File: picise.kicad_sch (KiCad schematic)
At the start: 22 parts, among them J1 SSW-120-22-G-D-RA, J2 SMA jack, J3 TSW-120-08-G-D-RA, J4 Conn_01x02, U1 CAT24C256, U2 MAX-M10S

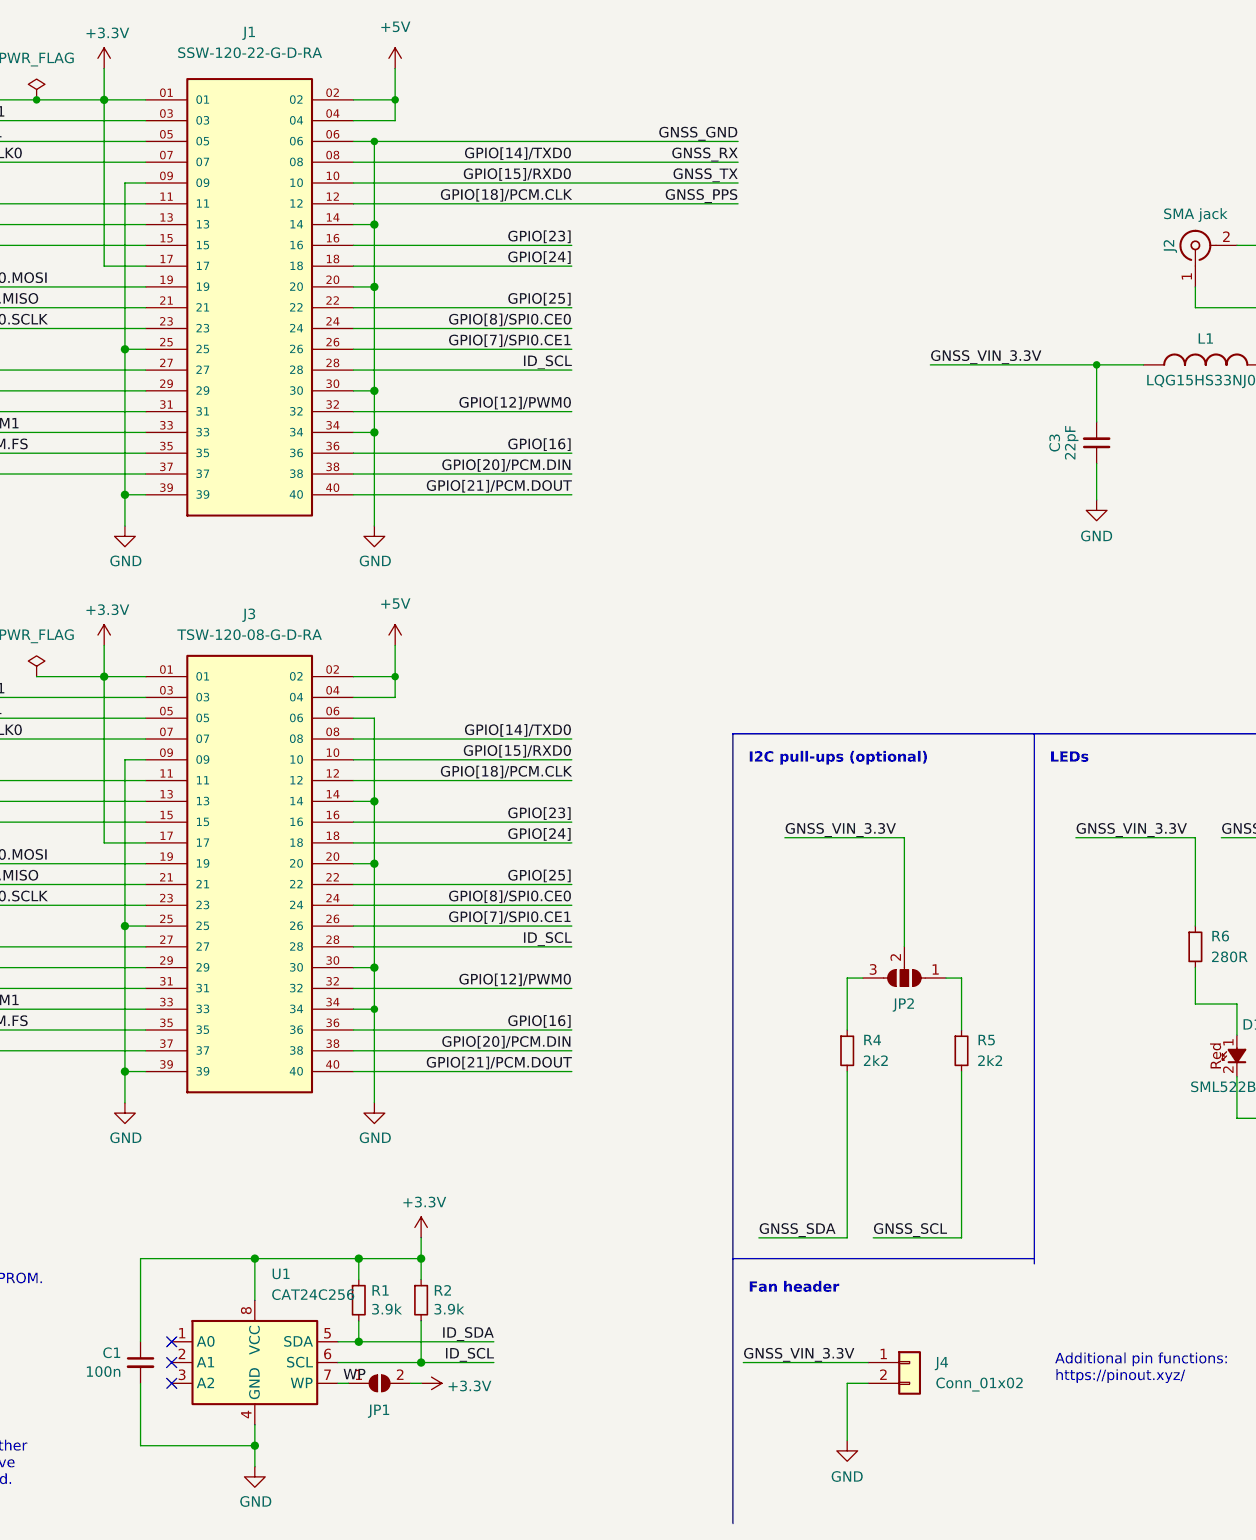
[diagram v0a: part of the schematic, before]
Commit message: added BOM
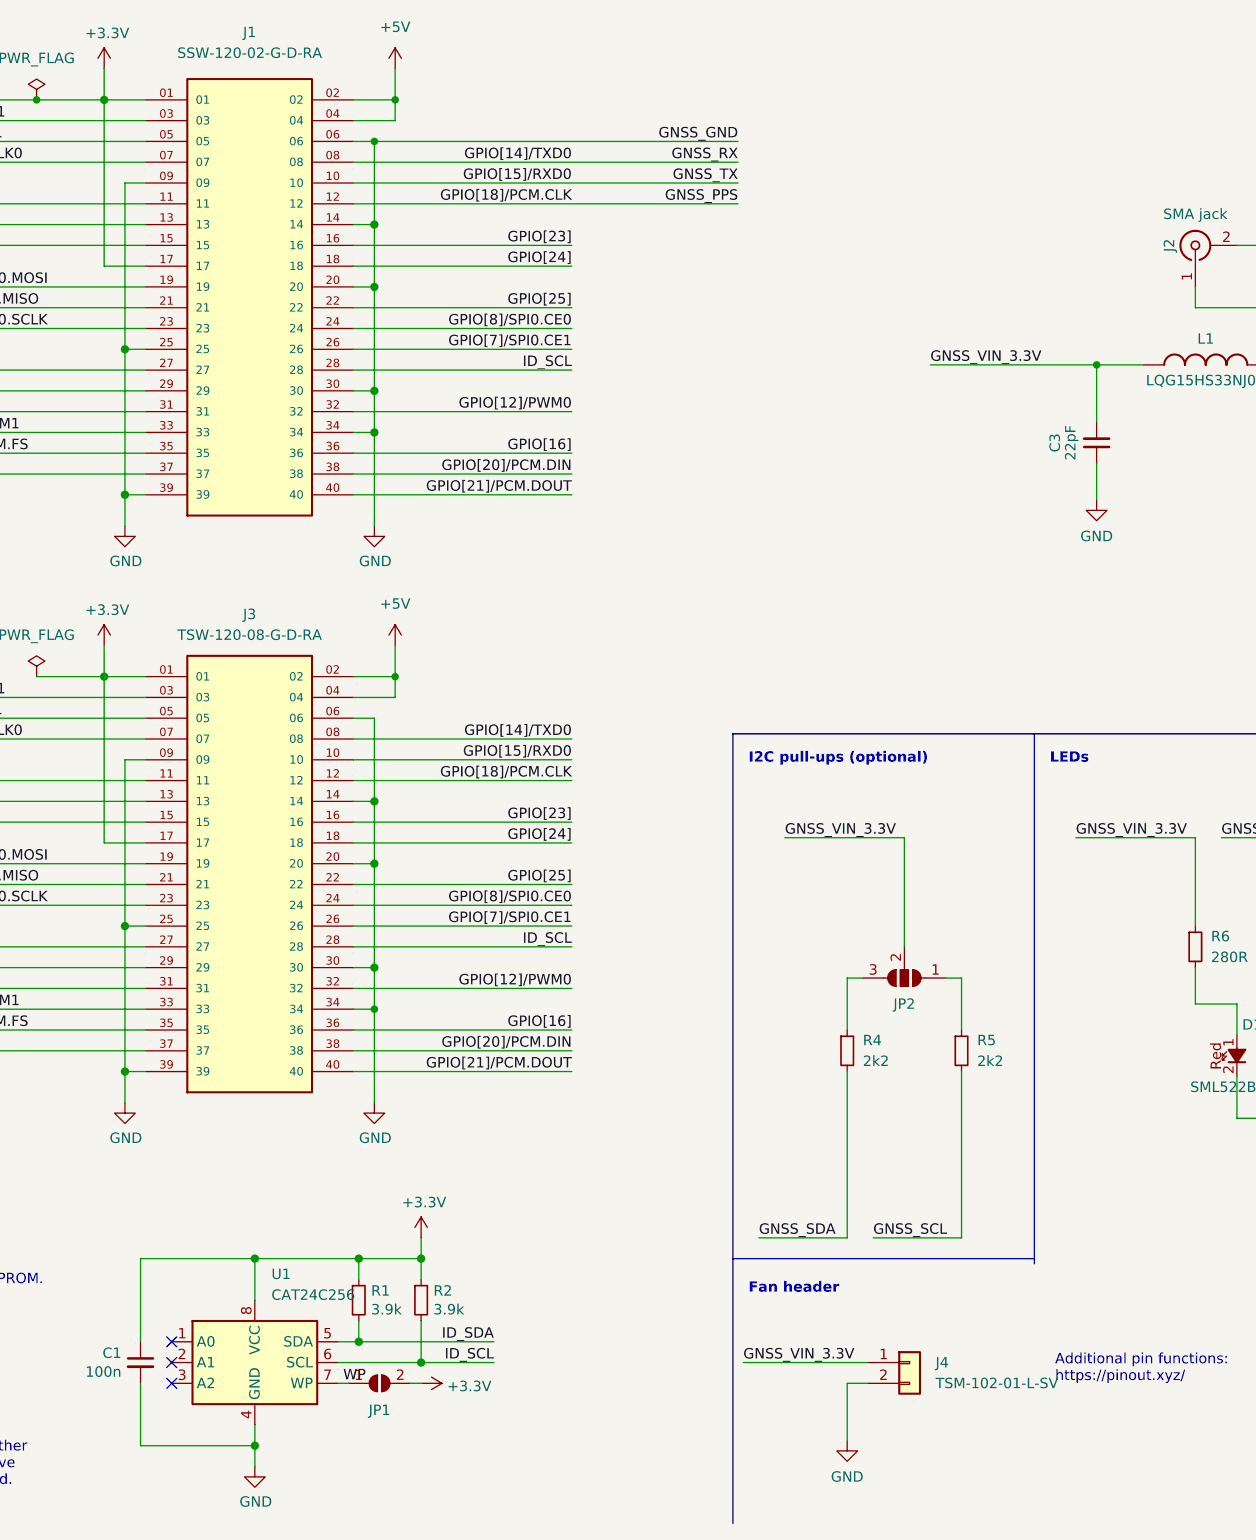
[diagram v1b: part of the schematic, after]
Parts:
- C1: MPN (none) -> C0805C104J5RAC7800; Manufacturer (none) -> KEMET
- C2: MPN (none) -> C0805C105J4RAC7800; Manufacturer (none) -> KEMET
- C3: MPN (none) -> C0805C220J4GAC7800; Manufacturer (none) -> KEMET
- D2: footprint Capacitor_SMD:C_0805_2012Metric_Pad1.18x1.45mm_HandSolder -> Diode_SMD:D_0805_2012Metric; MPN (none) -> SD0805S040S0R5; Manufacturer (none) -> KYOCERA AVX
- J1: value SSW-120-22-G-D-RA -> SSW-120-02-G-D-RA
- J4: value Conn_01x02 -> TSM-102-01-L-SV; MPN (none) -> TSM-102-01-L-SV; Manufacturer (none) -> Samtec
- R1, R2: MPN (none) -> RK73H2ARTTD3901F; Manufacturer (none) -> KOA Speer
- R3: MPN (none) -> RK73H2ATTD6200F; Manufacturer (none) -> KOA Speer
- R4, R5: MPN (none) -> RK73H2ATTD2201F; Manufacturer (none) -> KOA Speer
- R6: MPN (none) -> RK73H2ATTD2800F; Manufacturer (none) -> KOA Speer
- R7: MPN (none) -> RK73H2ARTTD80R6F; Manufacturer (none) -> KOA Speer
- U2: MPN MAX-M10S -> MAX-M10S-00B
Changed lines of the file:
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@@
+      (effects (font (size 1.27 1.27)) hide)
+    )
+    (property "MPN" "C0805C104J5RAC7800" (id 4) (at 67.31 177.8 0)
+      (effects (font (size 1.27 1.27)) hide)
+    )
+    (property "Manufacturer" "KEMET" (id 5) (at 67.31 177.8 0)
       (effects (font (size 1.27 1.27)) hide)
     )
@@
       (effects (font (size 1.27 1.27)) hide)
     )
-    (property "MPN" "MAX-M10S" (id 5) (at 250.19 76.835 0)
+    (property "MPN" "MAX-M10S-00B" (id 5) (at 250.19 76.835 0)
       (effects (font (size 1.27 1.27)) hide)
     )
@@
       (effects (font (size 1.27 1.27)) hide)
     )
+    (property "MPN" "C0805C105J4RAC7800" (id 4) (at 261.62 148.59 0)
+      (effects (font (size 1.27 1.27)) hide)
+    )
+    (property "Manufacturer" "KEMET" (id 5) (at 261.62 148.59 0)
+      (effects (font (size 1.27 1.27)) hide)
+    )
     (pin "1")
     (pin "2")
@@
     )
     (property "Datasheet" "~" (id 3) (at 93.98 170.18 0)
+      (effects (font (size 1.27 1.27)) hide)
+    )
+    (property "MPN" "RK73H2ARTTD3901F" (id 4) (at 93.98 170.18 0)
+      (effects (font (size 1.27 1.27)) hide)
+    )
+    (property "Manufacturer" "KOA Speer" (id 5) (at 93.98 170.18 0)
       (effects (font (size 1.27 1.27)) hide)
     )
@@
     )
     (property "Datasheet" "~" (id 3) (at 101.6 170.18 0)
+      (effects (font (size 1.27 1.27)) hide)
+    )
+    (property "MPN" "RK73H2ARTTD3901F" (id 4) (at 101.6 170.18 0)
+      (effects (font (size 1.27 1.27)) hide)
+    )
+    (property "Manufacturer" "KOA Speer" (id 5) (at 101.6 170.18 0)
       (effects (font (size 1.27 1.27)) hide)
     )
@@
       (effects (font (size 1.27 1.27)) (justify right))
     )
-    (property "Footprint" "Capacitor_SMD:C_0805_2012Metric_Pad1.18x1.45mm_HandSolder" (id 2) (at 240.665 123.825 0)
+    (property "Footprint" "Diode_SMD:D_0805_2012Metric" (id 2) (at 240.665 123.825 0)
       (effects (font (size 1.27 1.27)) hide)
     )
     (property "Datasheet" "~" (id 3) (at 240.665 123.825 0)
+      (effects (font (size 1.27 1.27)) hide)
+    )
+    (property "MPN" "SD0805S040S0R5" (id 4) (at 240.665 123.825 0)
+      (effects (font (size 1.27 1.27)) hide)
+    )
+    (property "Manufacturer" "KYOCERA AVX" (id 5) (at 240.665 123.825 0)
       (effects (font (size 1.27 1.27)) hide)
     )
@@
     )
     (property "Datasheet" "~" (id 3) (at 167.64 139.7 0)
+      (effects (font (size 1.27 1.27)) hide)
+    )
+    (property "MPN" "RK73H2ATTD2201F" (id 4) (at 167.64 139.7 0)
+      (effects (font (size 1.27 1.27)) hide)
+    )
+    (property "Manufacturer" "KOA Speer" (id 5) (at 167.64 139.7 0)
       (effects (font (size 1.27 1.27)) hide)
     )
@@
       (effects (font (size 1.27 1.27)) (justify left))
     )
-    (property "Value" "Conn_01x02" (id 1) (at 164.465 180.3399 0)
+    (property "Value" "TSM-102-01-L-SV" (id 1) (at 164.465 180.3399 0)
       (effects (font (size 1.27 1.27)) (justify left))
     )
@@
     )
     (property "Datasheet" "~" (id 3) (at 161.29 177.8 0)
+      (effects (font (size 1.27 1.27)) hide)
+    )
+    (property "MPN" "TSM-102-01-L-SV" (id 4) (at 161.29 177.8 0)
+      (effects (font (size 1.27 1.27)) hide)
+    )
+    (property "Manufacturer" "Samtec" (id 5) (at 161.29 177.8 0)
       (effects (font (size 1.27 1.27)) hide)
     )
@@
       (effects (font (size 1.27 1.27)) hide)
     )
+    (property "MPN" "RK73H2ATTD2201F" (id 4) (at 153.67 139.7 0)
+      (effects (font (size 1.27 1.27)) hide)
+    )
+    (property "Manufacturer" "KOA Speer" (id 5) (at 153.67 139.7 0)
+      (effects (font (size 1.27 1.27)) hide)
+    )
     (pin "1")
     (pin "2")
@@
       (effects (font (size 1.27 1.27)) hide)
     )
+    (property "MPN" "RK73H2ATTD6200F" (id 4) (at 240.665 133.985 0)
+      (effects (font (size 1.27 1.27)) hide)
+    )
+    (property "Manufacturer" "KOA Speer" (id 5) (at 240.665 133.985 0)
+      (effects (font (size 1.27 1.27)) hide)
+    )
     (pin "1")
     (pin "2")
@@
     (in_bom yes) (on_board yes) (fields_autoplaced)
     (property "Reference" "J1" (id 0) (at 80.645 15.24 0))
-    (property "Value" "SSW-120-22-G-D-RA" (id 1) (at 80.645 17.78 0))
+    (property "Value" "SSW-120-02-G-D-RA" (id 1) (at 80.645 17.78 0))
     (property "Footprint" "Connector_Header_Samtec:SAMTEC_SSW-120-22-G-D-RA" (id 2) (at 65.405 87.63 0)
       (effects (font (size 1.27 1.27)) (justify left bottom) hide)
@@
       (effects (font (size 1.27 1.27)) hide)
     )
+    (property "MPN" "C0805C220J4GAC7800" (id 4) (at 184.15 65.405 0)
+      (effects (font (size 1.27 1.27)) hide)
+    )
+    (property "Manufacturer" "KEMET" (id 5) (at 184.15 65.405 0)
+      (effects (font (size 1.27 1.27)) hide)
+    )
     (pin "1")
     (pin "2")
@@
     )
     (property "Datasheet" "~" (id 3) (at 196.215 127 0)
+      (effects (font (size 1.27 1.27)) hide)
+    )
+    (property "MPN" "RK73H2ATTD2800F" (id 4) (at 196.215 127 0)
+      (effects (font (size 1.27 1.27)) hide)
+    )
+    (property "Manufacturer" "KOA Speer" (id 5) (at 196.215 127 0)
       (effects (font (size 1.27 1.27)) hide)
     )
@@
     )
     (property "Datasheet" "~" (id 3) (at 210.82 127 0)
+      (effects (font (size 1.27 1.27)) hide)
+    )
+    (property "MPN" "RK73H2ARTTD80R6F" (id 4) (at 210.82 127 0)
+      (effects (font (size 1.27 1.27)) hide)
+    )
+    (property "Manufacturer" "KOA Speer" (id 5) (at 210.82 127 0)
       (effects (font (size 1.27 1.27)) hide)
     )
@@
     )
     (path "/ac297a88-9287-4a9f-bd67-7f1f8817f242"
-      (reference "D2") (unit 1) (value "0.5A 40V 420mV") (footprint "Capacitor_SMD:C_0805_2012Metric_Pad1.18x1.45mm_HandSolder")
+      (reference "D2") (unit 1) (value "0.5A 40V 420mV") (footprint "Diode_SMD:D_0805_2012Metric")
     )
     (path "/df883408-807c-458f-924a-53ad59baf3c9"
-      (reference "J1") (unit 1) (value "SSW-120-22-G-D-RA") (footprint "Connector_Header_Samtec:SAMTEC_SSW-120-22-G-D-RA")
+      (reference "J1") (unit 1) (value "SSW-120-02-G-D-RA") (footprint "Connector_Header_Samtec:SAMTEC_SSW-120-22-G-D-RA")
     )
     (path "/e38330bb-c7ad-4477-8444-fab35c01fdca"
@@
     )
     (path "/b5bc33c5-f237-4113-82dc-9833ded1e077"
-      (reference "J4") (unit 1) (value "Conn_01x02") (footprint "Connector_PinHeader_2.54mm:PinHeader_1x02_P2.54mm_Vertical_SMD_Pin1Left")
+      (reference "J4") (unit 1) (value "TSM-102-01-L-SV") (footprint "Connector_PinHeader_2.54mm:PinHeader_1x02_P2.54mm_Vertical_SMD_Pin1Left")
     )
     (path "/43e66c4c-de75-44f8-8171-19825b035cbb"

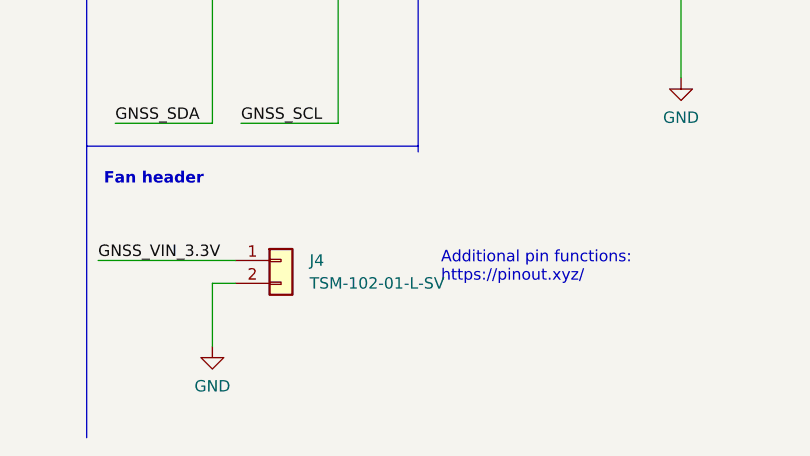
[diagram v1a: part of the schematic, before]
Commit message: BOM tweak
3-pin to account for left pin 1
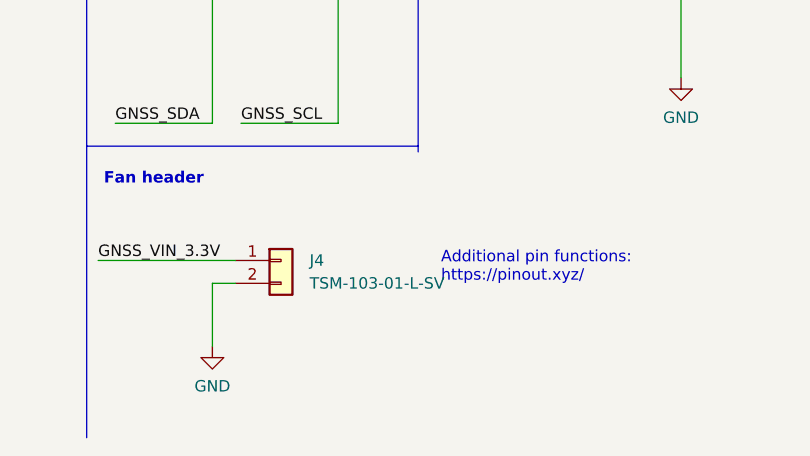
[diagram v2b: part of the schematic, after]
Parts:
- J4: value TSM-102-01-L-SV -> TSM-103-01-L-SV
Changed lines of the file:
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@@
       (effects (font (size 1.27 1.27)) (justify left))
     )
-    (property "Value" "TSM-102-01-L-SV" (id 1) (at 164.465 180.3399 0)
+    (property "Value" "TSM-103-01-L-SV" (id 1) (at 164.465 180.3399 0)
       (effects (font (size 1.27 1.27)) (justify left))
     )
@@
     )
     (path "/b5bc33c5-f237-4113-82dc-9833ded1e077"
-      (reference "J4") (unit 1) (value "TSM-102-01-L-SV") (footprint "Connector_PinHeader_2.54mm:PinHeader_1x02_P2.54mm_Vertical_SMD_Pin1Left")
+      (reference "J4") (unit 1) (value "TSM-103-01-L-SV") (footprint "Connector_PinHeader_2.54mm:PinHeader_1x02_P2.54mm_Vertical_SMD_Pin1Left")
     )
     (path "/43e66c4c-de75-44f8-8171-19825b035cbb"

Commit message: rev2 prep
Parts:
- removed C3: 22pF, Capacitor_SMD:C_0805_2012Metric_Pad1.18x1.45mm_HandSolder, symbol Device:C_Small
- removed J3: TSW-120-08-G-D-RA, Connector_Header_Samtec:SAMTEC_TSW-120-08-G-D-RA, symbol Connector_Header_Samtec:TSW-120-08-G-D-RA
- removed L1: LQG15HS33NJ02D, Inductor_SMD_Murata:INDC1005X55N, symbol Inductor_SMD_Murata:LQG15HS33NJ02D
- added C?: 47pF, symbol Device:C_Small
- added L?: 47nH, symbol Device:L_Small
- added R?: 10R, symbol Device:R_Small
- added SW?: ANT_ACTIVE, symbol Switch:SW_SPST
- J2: value SMA jack -> ANT_SMA
- J?: renamed from J1; value SSW-120-02-G-D-RA -> SSQ-120-03_GPIO; footprint Connector_Header_Samtec:SAMTEC_SSW-120-22-G-D-RA -> Connector_Header_Samtec:SAMTEC_SSQ-120-03-G-D_Pi_Annotated_PPS; symbol Connector_Header_Samtec:SSW-120-22-G-D-RA -> Connector_Header_Samtec:SSQ-120-03_GPIO
- R6: value 280R -> 330R
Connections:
- net GNSS_RF_IN: now also C?.2; no longer J2.1
- net at U2.14 (VCC_RF): now also R?.2
- net ~{GNSS_SAFEBOOT}: now reaches U2.18 (~{SAFEBOOT})
- net ~{GNSS_RESET}: now reaches U2.9 (~{RESET})
- net GNSS_LNA_EN: no longer names the net of U2.13 (LNA_EN)
- new net: C?.1, J2.1, SW?.1 (A)
- new net: L?.1, SW?.2 (B)
- new net: L?.2, R?.1
- no-connect marks 9 -> 6
